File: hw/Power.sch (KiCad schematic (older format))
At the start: 5 parts

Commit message: Add connectors
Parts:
- J3: renamed from J?; footprint (none) -> TerminalBlock:TerminalBlock_Altech_AK300-2_P5.00mm
- gave numbers to parts that had none: 3
- renumbered POLYFUSE to POLYFUSE1
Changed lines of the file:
@@
 $EndDescr
 $Comp
-L Connector:Conn_01x01_Female J?
+L Connector:Conn_01x01_Female J3
 U 1 1 5F900653
 P 3350 3200
-F 0 "J?" H 3242 2975 50  0000 C CNN
+F 0 "J3" H 3242 2975 50  0000 C CNN
 F 1 "Conn_01x01_Female" H 3242 3066 50  0000 C CNN
-F 2 "" H 3350 3200 50  0001 C CNN
+F 2 "TerminalBlock:TerminalBlock_Altech_AK300-2_P5.00mm" H 3350 3200 50  0001 C CNN
 F 3 "~" H 3350 3200 50  0001 C CNN
 	1    3350 3200
@@
 $EndComp
 $Comp
-L power:+24V #PWR?
+L power:+24V #PWR0113
 U 1 1 5F901264
 P -3850 -3500
-F 0 "#PWR?" H -3850 -3650 50  0001 C CNN
+F 0 "#PWR0113" H -3850 -3650 50  0001 C CNN
 F 1 "+24V" H -3835 -3327 50  0000 C CNN
 F 2 "" H -3850 -3500 50  0001 C CNN
@@
 $EndComp
 $Comp
-L SS34:SS34 D?
+L SS34:SS34 D4
 U 1 1 5F904EDE
 P 4000 3200
-F 0 "D?" H 4000 3417 50  0000 C CNN
+F 0 "D4" H 4000 3417 50  0000 C CNN
 F 1 "SS34" H 4000 3326 50  0000 C CNN
 F 2 "DIOM7959X265N" H 3750 2950 50  0001 L BNN
@@
 	4000 3450 4000 3550
 $Comp
-L power:GND #PWR?
+L power:GND #PWR0114
 U 1 1 5F9055D3
 P 4000 3550
-F 0 "#PWR?" H 4000 3300 50  0001 C CNN
+F 0 "#PWR0114" H 4000 3300 50  0001 C CNN
 F 1 "GND" H 4005 3377 50  0000 C CNN
 F 2 "" H 4000 3550 50  0001 C CNN
@@
 From optocoupler
 $Comp
-L Device:R POLYFUSE
+L Device:R POLYFUSE1
 U 1 1 5F9070EE
 P 4550 3200
-F 0 "POLYFUSE" V 4757 3200 50  0000 C CNN
+F 0 "POLYFUSE1" V 4757 3200 50  0000 C CNN
 F 1 "24V 1A" V 4650 3200 50  0000 C CNN
 F 2 "Resistor_SMD:R_1206_3216Metric" V 4480 3200 50  0001 C CNN
@@
 	4900 3200 4900 3450
 $Comp
-L Device:C C?
+L Device:C C4
 U 1 1 5F90869A
 P 5650 3600
-F 0 "C?" H 5765 3646 50  0000 L CNN
+F 0 "C4" H 5765 3646 50  0000 L CNN
 F 1 "10u/50V" H 5765 3555 50  0000 L CNN
 F 2 "" H 5688 3450 50  0001 C CNN
@@
 $EndComp
 $Comp
-L power:+24V #PWR?
+L power:+24V #PWR0115
 U 1 1 5F909B7A
 P 4900 2950
-F 0 "#PWR?" H 4900 2800 50  0001 C CNN
+F 0 "#PWR0115" H 4900 2800 50  0001 C CNN
 F 1 "+24V" H 4915 3123 50  0000 C CNN
 F 2 "" H 4900 2950 50  0001 C CNN
@@
 $EndComp
 $Comp
-L 1SMB5935BT3G:1SMB5935BT3G D?
+L 1SMB5935BT3G:1SMB5935BT3G D5
 U 1 1 5F90C9CC
 P 4900 3650
-F 0 "D?" V 4946 3570 50  0000 R CNN
+F 0 "D5" V 4946 3570 50  0000 R CNN
 F 1 "1SMB5935BT3G" V 4855 3570 50  0000 R CNN
 F 2 "1SMB5935BT3G:DIOM5436X247N" H 4300 3400 50  0001 L BNN

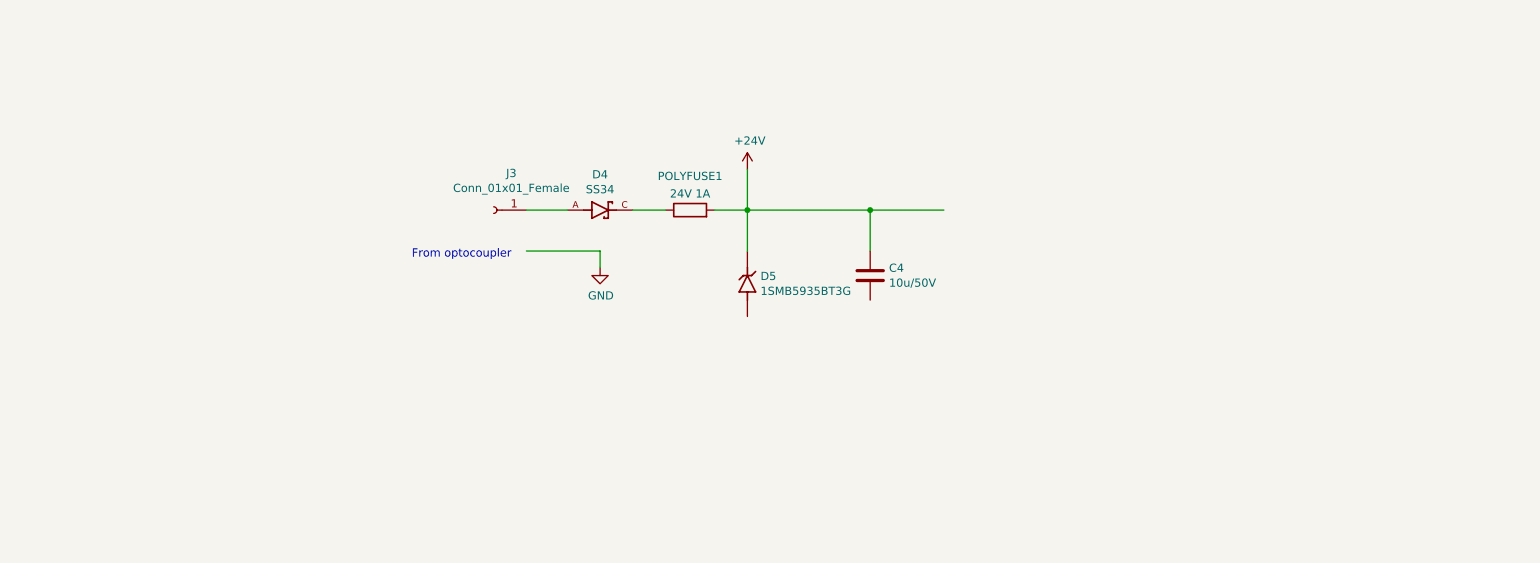
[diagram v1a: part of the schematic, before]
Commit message: Update some packages, add 3D models
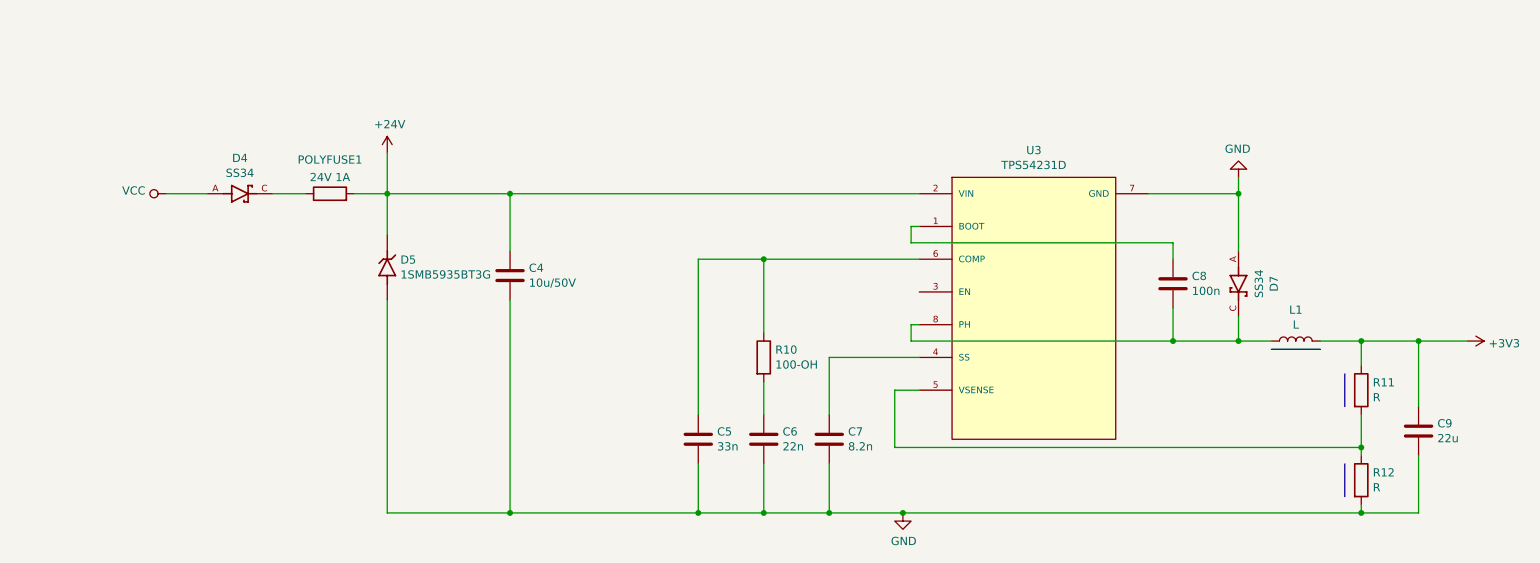
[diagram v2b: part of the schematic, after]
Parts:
- removed J3: Conn_01x01_Female, TerminalBlock:TerminalBlock_Altech_AK300-2_P5.00mm, symbol Connector:Conn_01x01_Female
- added C5: 33n, Capacitor_SMD:C_0603_1608Metric, symbol Device:C
- added C6: 22n, Capacitor_SMD:C_0603_1608Metric, symbol Device:C
- added C7: 8.2n, Capacitor_SMD:C_0603_1608Metric, symbol Device:C
- added C8: 100n, Capacitor_SMD:C_0603_1608Metric, symbol Device:C
- added C9: 22u, Capacitor_SMD:C_0603_1608Metric, symbol Device:C
- added D7: SS34, DIOM7959X265N, symbol SS34:SS34
- added L1: L, symbol Device:L
- added R10: 100-OH, Resistor_SMD:R_0603_1608Metric, symbol Device:R
- added R11, R12: R, Resistor_SMD:R_0603_1608Metric, symbol Device:R
- added U3: TPS54231D, SOIC127P599X175-8N, symbol TPS54231D:TPS54231D
- C4: footprint (none) -> Capacitor_SMD:C_0603_1608Metric; LCSC_ID (none) -> C13585
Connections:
- net labels added: +3V3, VCC
- wire segments 10 -> 53
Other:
- note removed: "From optocoupler"
- moved on the sheet: C4, D4, D5, POLYFUSE1

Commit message: Routing schema
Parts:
- C4: footprint Capacitor_SMD:C_0603_1608Metric -> Capacitor_SMD:C_1206_3216Metric
- D4, D7: footprint DIOM7959X265N -> SS34:SMA
- L1: footprint (none) -> Inductor_SMD:L_TDK_SLF7045
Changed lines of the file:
@@
 F 0 "C4" H 3565 3646 50  0000 L CNN
 F 1 "10u/50V" H 3565 3555 50  0000 L CNN
-F 2 "Capacitor_SMD:C_0603_1608Metric" H 3488 3450 50  0001 C CNN
+F 2 "Capacitor_SMD:C_1206_3216Metric" H 3488 3450 50  0001 C CNN
 F 3 "~" H 3450 3600 50  0001 C CNN
 F 4 "C13585" H 3450 3600 50  0001 C CNN "LCSC_ID"
@@
 F 0 "D4" H 1800 3317 50  0000 C CNN
 F 1 "SS34" H 1800 3226 50  0000 C CNN
-F 2 "DIOM7959X265N" H 1550 2850 50  0001 L BNN
+F 2 "SS34:SMA" H 1550 2850 50  0001 L BNN
 F 3 "https://www.snapeda.com/parts/SS34/ON%20Semiconductor/datasheet/" H 1800 3100 50  0001 L BNN
 F 4 "https://www.snapeda.com/parts/SS34/ON%20Semiconductor/view-part/?ref=search&t=SS34" H 1750 2750 50  0001 C CNN "Source"
@@
 F 0 "D7" H 7900 3867 50  0000 C CNN
 F 1 "SS34" H 7900 3776 50  0000 C CNN
-F 2 "DIOM7959X265N" H 7650 3400 50  0001 L BNN
+F 2 "SS34:SMA" H 7650 3400 50  0001 L BNN
 F 3 "https://www.snapeda.com/parts/SS34/ON%20Semiconductor/datasheet/" H 7900 3650 50  0001 L BNN
 F 4 "https://www.snapeda.com/parts/SS34/ON%20Semiconductor/view-part/?ref=search&t=SS34" H 7850 3300 50  0001 C CNN "Source"
@@
 F 0 "L1" V 8440 4000 50  0000 C CNN
 F 1 "L" V 8349 4000 50  0000 C CNN
-F 2 "" H 8250 4000 50  0001 C CNN
+F 2 "Inductor_SMD:L_TDK_SLF7045" H 8250 4000 50  0001 C CNN
 F 3 "~" H 8250 4000 50  0001 C CNN
 	1    8250 4000

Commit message: Routing board
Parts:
- R11: value R -> 4k7
- R12: value R -> 15k
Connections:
- net +24V: no longer C4.1, D5.C, POLYFUSE1.2, U3.2 (VIN)
- new net: C4.1, D5.C, POLYFUSE1.2, U3.2 (VIN)
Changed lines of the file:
@@
 Wire Wire Line
 	2500 3100 2700 3100
-Wire Wire Line
-	2700 3100 2700 2850
 Connection ~ 2700 3100
 Wire Wire Line
@@
 F 4 "C13585" H 3450 3600 50  0001 C CNN "LCSC_ID"
 	1    3450 3600
-	1    0    0    -1
-$EndComp
-$Comp
-L power:+24V #PWR0115
-U 1 1 5F909B7A
-P 2700 2850
-F 0 "#PWR0115" H 2700 2700 50  0001 C CNN
-F 1 "+24V" H 2715 3023 50  0000 C CNN
-F 2 "" H 2700 2850 50  0001 C CNN
-F 3 "" H 2700 2850 50  0001 C CNN
-	1    2700 2850
 	1    0    0    -1
 $EndComp
@@
 P 8650 4300
 F 0 "R11" H 8720 4346 50  0000 L CNN
-F 1 "R" H 8720 4255 50  0000 L CNN
+F 1 "4k7" H 8720 4255 50  0000 L CNN
 F 2 "Resistor_SMD:R_0603_1608Metric" V 8580 4300 50  0001 C CNN
 F 3 "~" H 8650 4300 50  0001 C CNN
@@
 P 8650 4850
 F 0 "R12" H 8720 4896 50  0000 L CNN
-F 1 "R" H 8720 4805 50  0000 L CNN
+F 1 "15k" H 8720 4805 50  0000 L CNN
 F 2 "Resistor_SMD:R_0603_1608Metric" V 8580 4850 50  0001 C CNN
 F 3 "~" H 8650 4850 50  0001 C CNN
@@
 Wire Bus Line
 	8100 4050 8400 4050
+Wire Wire Line
+	3450 5050 4600 5050
+Wire Wire Line
+	3450 3100 5950 3100
+Connection ~ 5850 5050
+Wire Wire Line
+	5850 5050 8650 5050
 Wire Bus Line
 	8550 4750 8550 4950
 Wire Bus Line
 	8550 4200 8550 4400
-Wire Wire Line
-	3450 5050 4600 5050
-Wire Wire Line
-	3450 3100 5950 3100
-Connection ~ 5850 5050
-Wire Wire Line
-	5850 5050 8650 5050
 $EndSCHEMATC
